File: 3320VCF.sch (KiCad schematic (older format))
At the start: 44 parts, among them J1 Conn_02x05_Odd_Even, J2 F_CV, J3 Audio_in, J4 Q_CV, J5 Audio_out, U1 TL074, U2 v3320

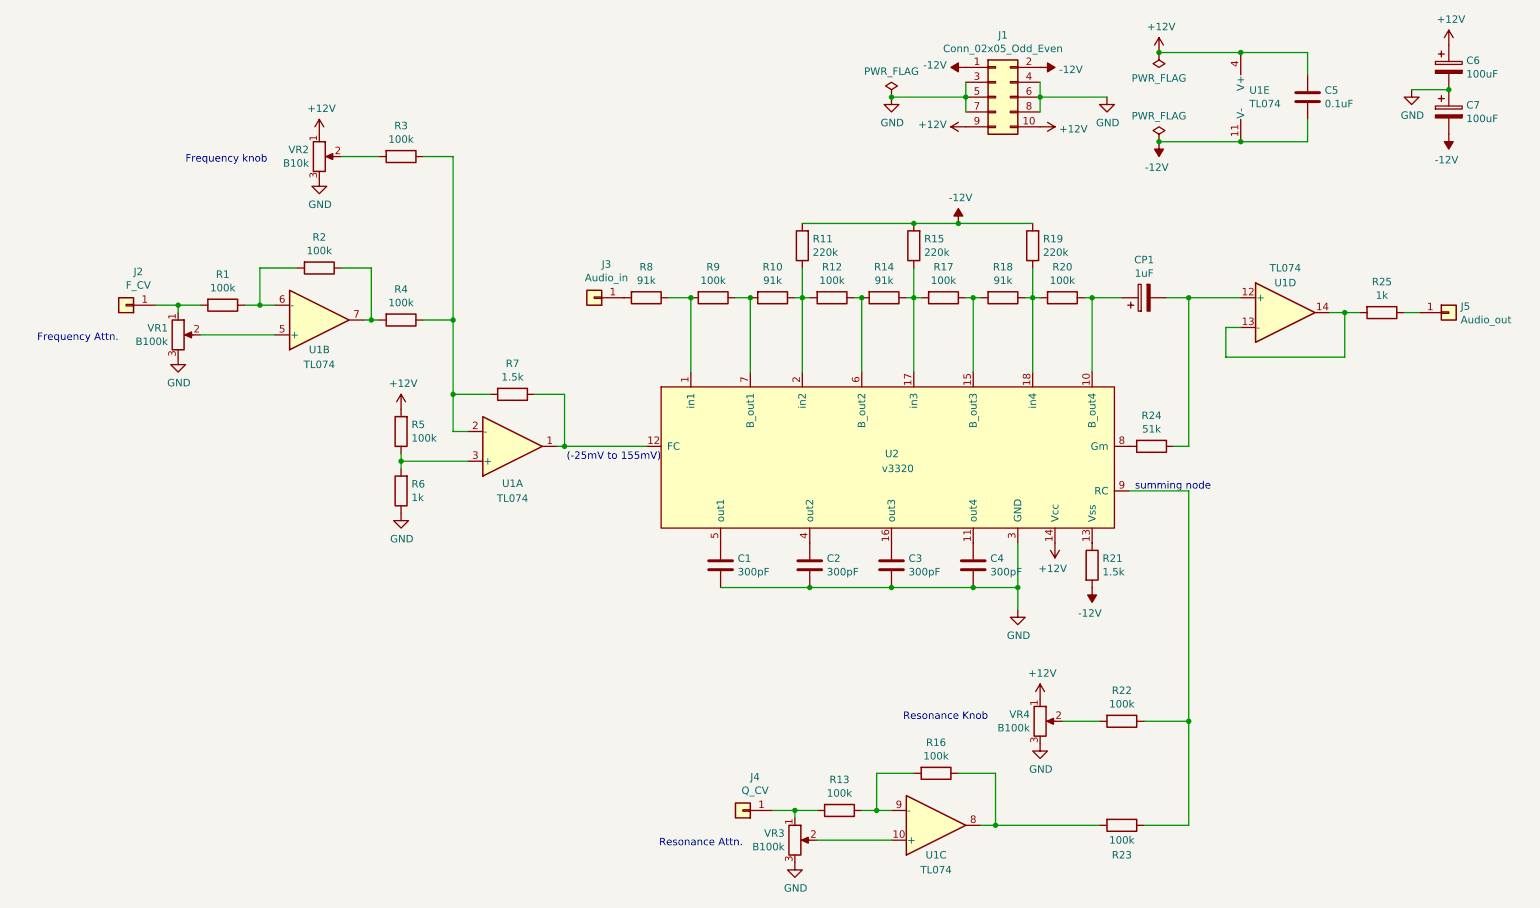
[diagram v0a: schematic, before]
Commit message: Improved the schematic: - fixed bugs in the pin orders of pots. - appened power reversal protection.
PCB design version 2, included front panel also.
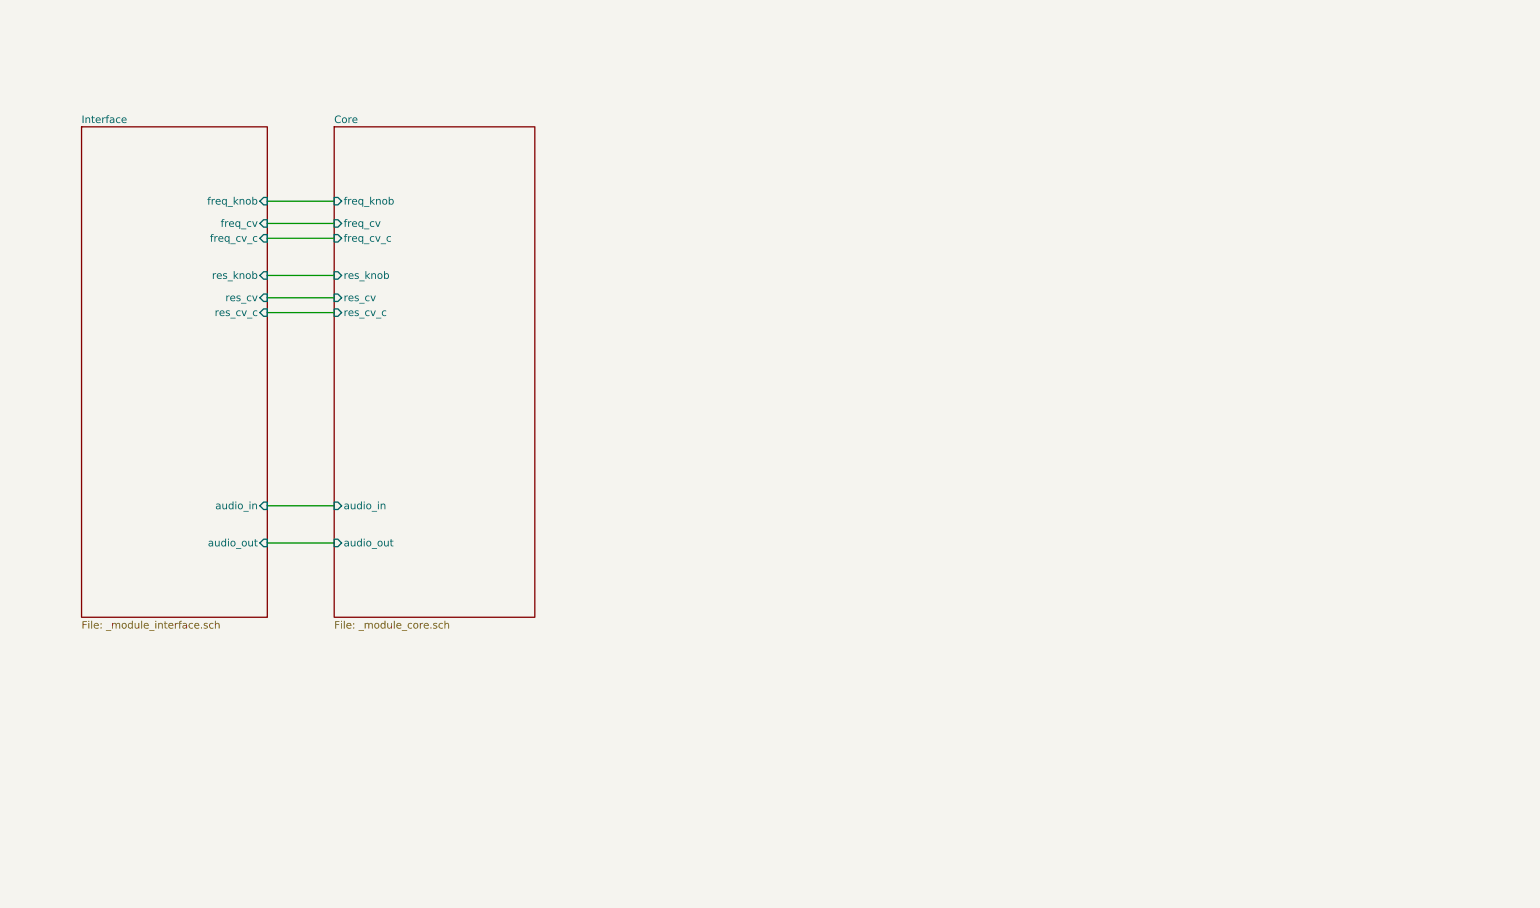
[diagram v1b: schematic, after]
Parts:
- removed C1, C2, C3, C4: 300pF, Capacitor_THT:C_Axial_L5.1mm_D3.1mm_P7.50mm_Horizontal, symbol Device:C
- removed C5: 0.1uF, Capacitor_THT:C_Axial_L5.1mm_D3.1mm_P7.50mm_Horizontal, symbol Device:C
- removed C6, C7: 100uF, Capacitor_THT:CP_Radial_D6.3mm_P2.50mm, symbol Device:CP
- removed CP1: 1uF, Capacitor_THT:CP_Radial_D5.0mm_P2.50mm, symbol Device:CP
- removed J1: Conn_02x05_Odd_Even, Connector_PinHeader_2.54mm:PinHeader_2x05_P2.54mm_Horizontal, symbol Connector_Generic:Conn_02x05_Odd_Even
- removed J2: F_CV, Connector_PinHeader_2.54mm:PinHeader_1x01_P2.54mm_Vertical, symbol Connector_Generic:Conn_01x01
- removed J3: Audio_in, Connector_PinHeader_2.54mm:PinHeader_1x01_P2.54mm_Vertical, symbol Connector_Generic:Conn_01x01
- removed J4: Q_CV, Connector_PinHeader_2.54mm:PinHeader_1x01_P2.54mm_Vertical, symbol Connector_Generic:Conn_01x01
- removed J5: Audio_out, Connector_PinHeader_2.54mm:PinHeader_1x01_P2.54mm_Vertical, symbol Connector_Generic:Conn_01x01
- removed R1, R12, R13, R16, R17, R2, R20, R22, R23, R3, R4, R5, R9: 100k, Resistor_THT:R_Axial_DIN0207_L6.3mm_D2.5mm_P7.62mm_Horizontal, symbol Device:R
- removed R10, R14, R18, R8: 91k, Resistor_THT:R_Axial_DIN0207_L6.3mm_D2.5mm_P7.62mm_Horizontal, symbol Device:R
- removed R11, R15, R19: 220k, Resistor_THT:R_Axial_DIN0207_L6.3mm_D2.5mm_P7.62mm_Horizontal, symbol Device:R
- removed R21, R7: 1.5k, Resistor_THT:R_Axial_DIN0207_L6.3mm_D2.5mm_P7.62mm_Horizontal, symbol Device:R
- removed R24: 51k, Resistor_THT:R_Axial_DIN0207_L6.3mm_D2.5mm_P7.62mm_Horizontal, symbol Device:R
- removed R25, R6: 1k, Resistor_THT:R_Axial_DIN0207_L6.3mm_D2.5mm_P7.62mm_Horizontal, symbol Device:R
- removed U1: TL074, Package_DIP:DIP-14_W7.62mm, symbol Amplifier_Operational:TL074
- removed U2: v3320, 3320VCF:DIP-18_700_ELL, symbol mylib:v3320
- removed VR1, VR3, VR4: B100k, Potentiometer_THT:Potentiometer_Alps_RK097_Single_Horizontal, symbol Device:R_POT
- removed VR2: B10k, Potentiometer_THT:Potentiometer_Alps_RK097_Single_Horizontal, symbol Device:R_POT
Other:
- note removed: "(-25mV to 155mV)"
- note removed: "Frequency Attn."
- note removed: "Frequency knob"
- note removed: "Resonance Attn."
- note removed: "Resonance Knob"
- note removed: "summing node"
